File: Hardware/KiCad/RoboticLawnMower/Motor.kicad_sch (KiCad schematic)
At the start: 7 parts, among them J1 MOTOR, U1 INA233

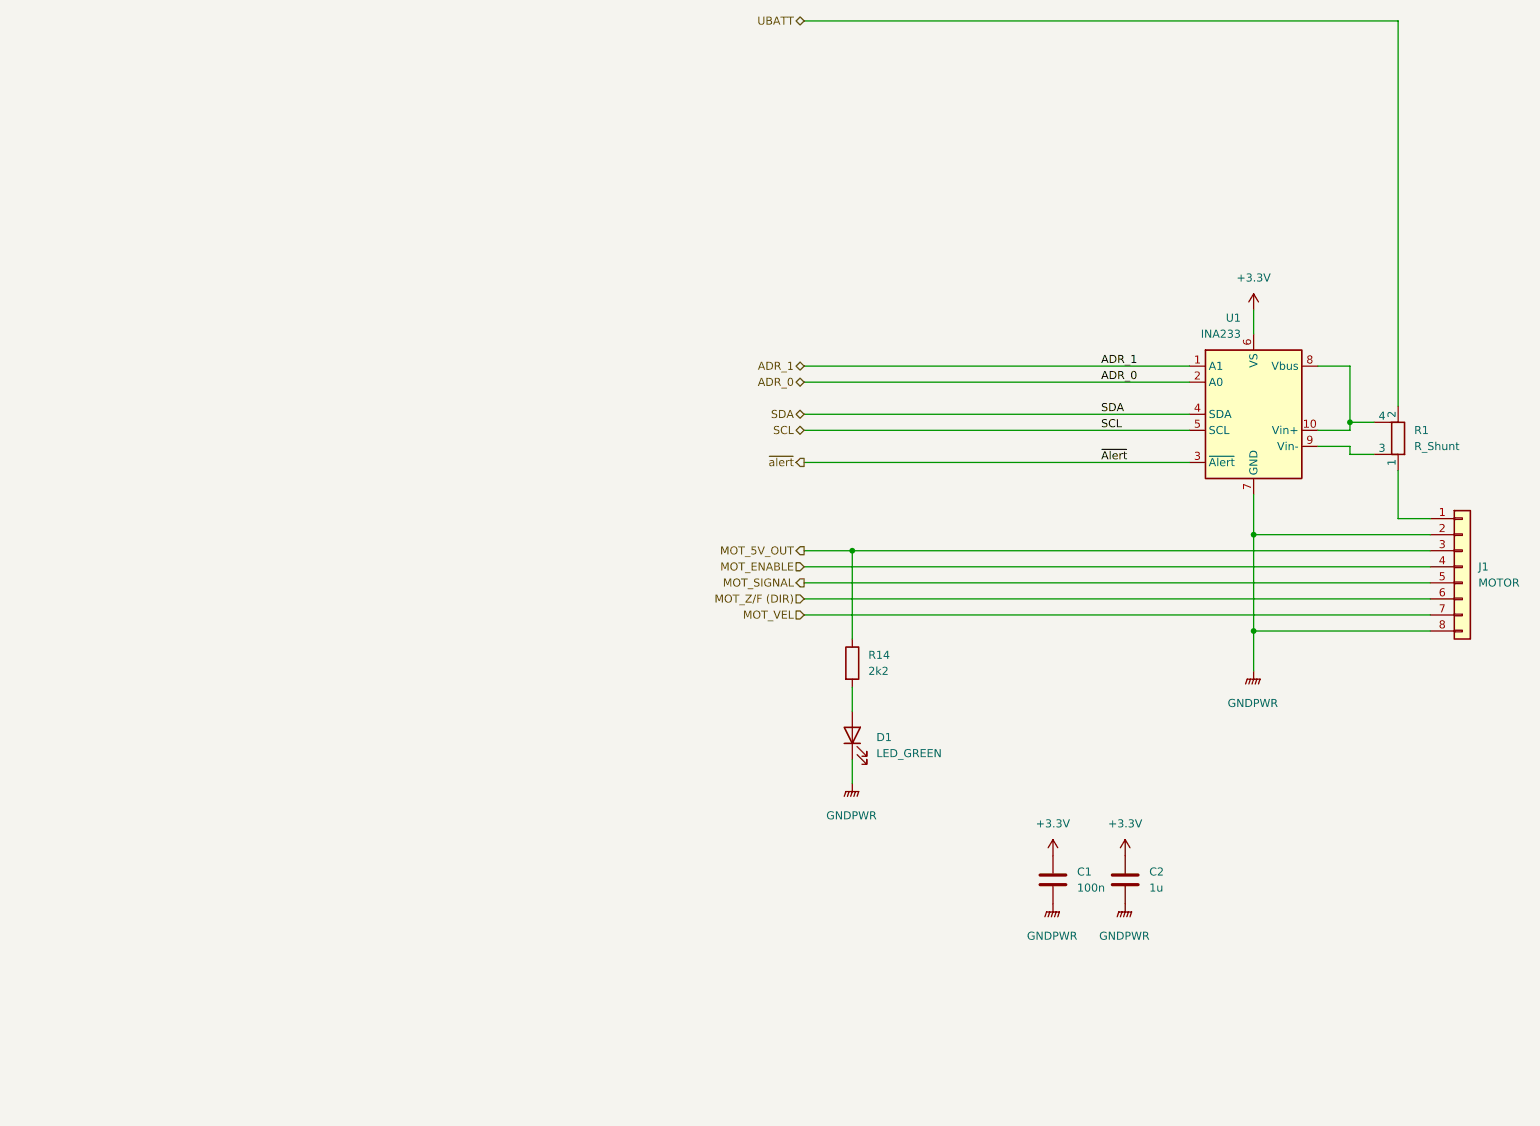
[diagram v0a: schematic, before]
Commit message: Redesign: - Controller - I2C pinning geändert - uvm
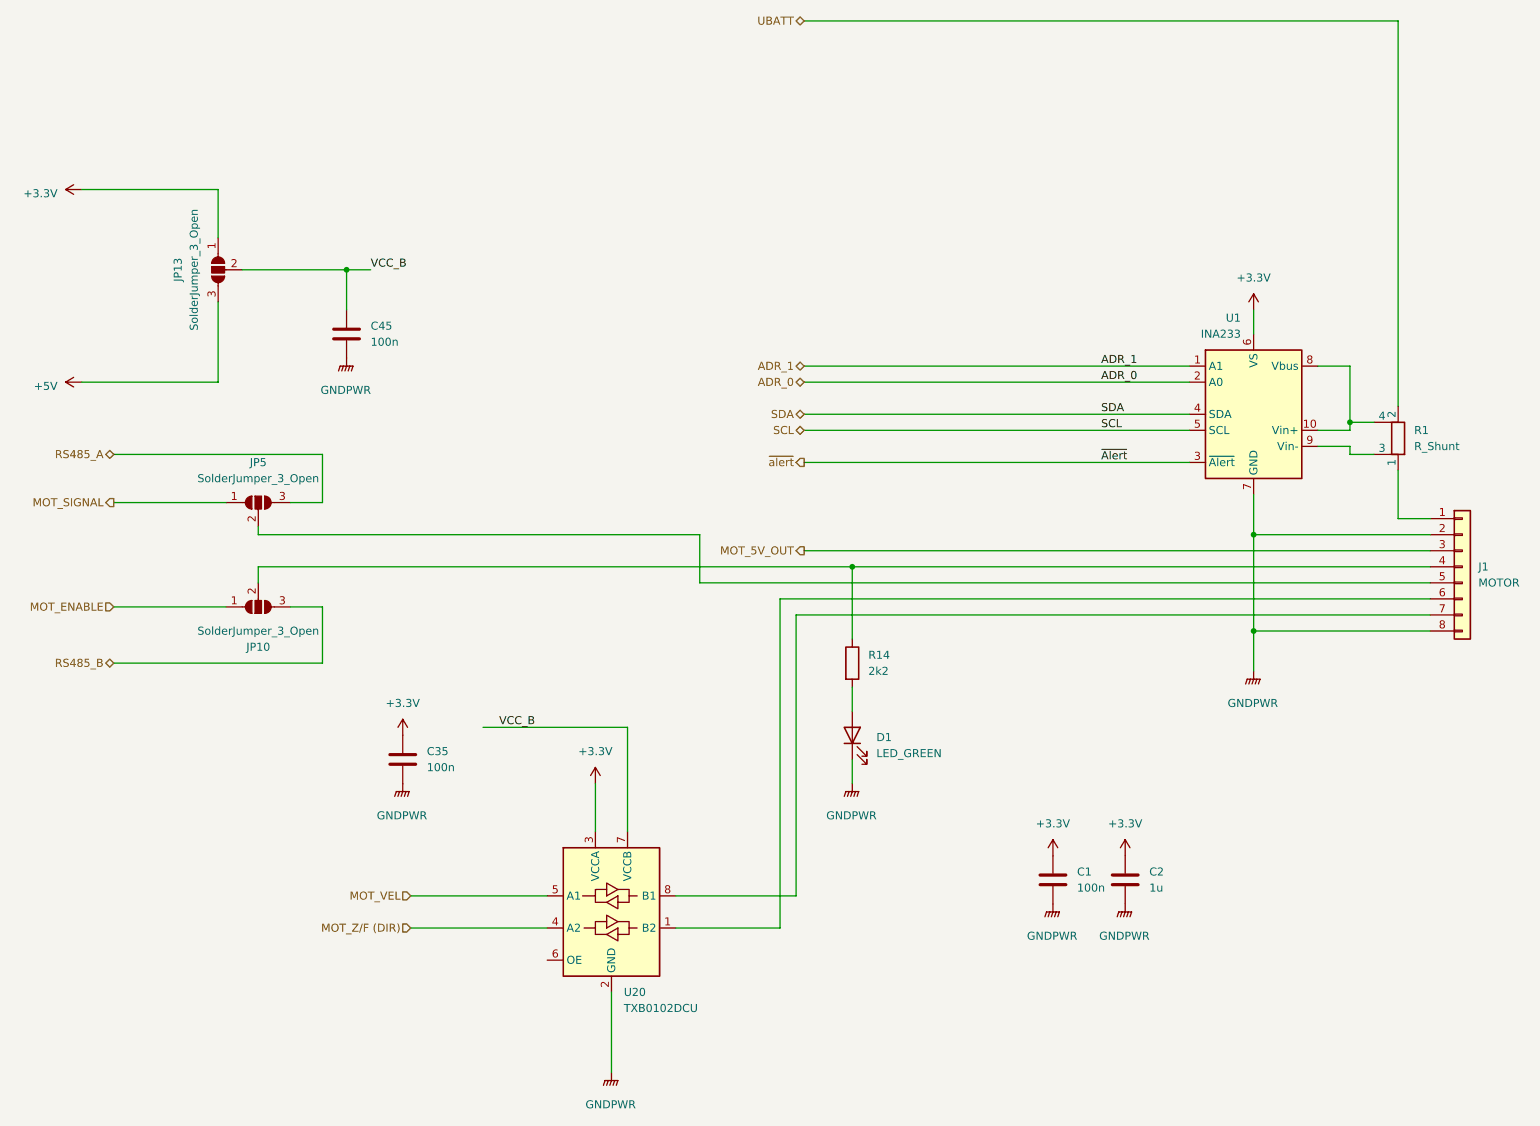
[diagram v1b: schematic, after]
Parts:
- added C35, C45: 100n, Capacitor_SMD:C_0603_1608Metric, symbol Device:C
- added JP10, JP13, JP5: SolderJumper_3_Open, Jumper:SolderJumper-3_P1.3mm_Open_RoundedPad1.0x1.5mm, symbol Jumper:SolderJumper_3_Open
- added U20: TXB0102DCU, Package_SO:VSSOP-8_2.4x2.1mm_P0.5mm, symbol Logic_LevelTranslator:TXB0102DCU
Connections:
- net +3.3V: now also C35.1, JP13.1 (A), U20.3 (VCCA)
- net GNDPWR: now also C35.2, C45.2, U20.2 (GND)
- net MOT_5V_OUT: no longer R14.1
- net MOT_ENABLE: now also JP10.1 (A); no longer J1.4 (Pin_4)
- net MOT_SIGNAL: now also JP5.1 (A); no longer J1.5 (Pin_5)
- net MOT_VEL: now also U20.5 (A1); no longer J1.7 (Pin_7)
- net MOT_Z/F (DIR): now also U20.4 (A2); no longer J1.6 (Pin_6)
- new net: J1.5 (Pin_5), JP5.2 (C)
- new net: J1.4 (Pin_4), JP10.2 (C), R14.1
- new net: J1.6 (Pin_6), U20.1 (B2)
- new net: J1.7 (Pin_7), U20.8 (B1)
- new net +5V: JP13.3 (B)
- new net RS485_A: JP5.3 (B)
- new net RS485_B: JP10.3 (B)
- new net VCC_B: C45.1, JP13.2 (C), U20.7 (VCCB)

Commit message: Layout fertig, Gerber-Datei muss noch erzeugt werden.
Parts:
- renumbered C2 to C10, C35 to C39, C45 to C49, C1 to C9, D1 to D5, J1 to J5, JP10 to JP12, JP13 to JP17, JP5 to JP7, R14 to R18, R1 to R5, U1 to U13, U20 to U24
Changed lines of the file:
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@@
 		(dnp no)
 		(fields_autoplaced yes)
-		(property "Reference" "C45"
+		(property "Reference" "C49"
 			(at 134.62 110.4899 0)
 			(effects
@@
 		(dnp no)
 		(fields_autoplaced yes)
-		(property "Reference" "#PWR060"
+		(property "Reference" "#PWR064"
 			(at 210.82 187.96 0)
 			(effects
@@
 		(dnp no)
 		(fields_autoplaced yes)
-		(property "Reference" "JP5"
+		(property "Reference" "JP7"
 			(at 116.84 132.08 0)
 			(effects
@@
 		(dnp no)
 		(fields_autoplaced yes)
-		(property "Reference" "D1"
+		(property "Reference" "D5"
 			(at 214.63 175.5774 90)
 			(effects
@@
 		(dnp no)
 		(fields_autoplaced yes)
-		(property "Reference" "#PWR0188"
+		(property "Reference" "#PWR0192"
 			(at 130.81 120.65 0)
 			(effects
@@
 		(dnp no)
 		(fields_autoplaced yes)
-		(property "Reference" "#PWR0168"
+		(property "Reference" "#PWR0176"
 			(at 139.7 179.07 0)
 			(effects
@@
 		(dnp no)
 		(fields_autoplaced yes)
-		(property "Reference" "#PWR0163"
+		(property "Reference" "#PWR0167"
 			(at 92.71 119.38 0)
 			(effects
@@
 		(on_board yes)
 		(dnp no)
-		(property "Reference" "JP10"
+		(property "Reference" "JP12"
 			(at 116.84 161.29 0)
 			(effects
@@
 		(dnp no)
 		(fields_autoplaced yes)
-		(property "Reference" "#PWR0169"
+		(property "Reference" "#PWR0177"
 			(at 139.7 187.96 0)
 			(effects
@@
 		(dnp no)
 		(fields_autoplaced yes)
-		(property "Reference" "C35"
+		(property "Reference" "C39"
 			(at 143.51 177.7999 0)
 			(effects
@@
 		(dnp no)
 		(fields_autoplaced yes)
-		(property "Reference" "#PWR0114"
+		(property "Reference" "#PWR0138"
 			(at 242.57 207.01 0)
 			(effects
@@
 		(dnp no)
 		(fields_autoplaced yes)
-		(property "Reference" "#PWR067"
+		(property "Reference" "#PWR087"
 			(at 170.18 186.69 0)
 			(effects
@@
 		(dnp no)
 		(fields_autoplaced yes)
-		(property "Reference" "#PWR098"
+		(property "Reference" "#PWR0162"
 			(at 92.71 88.9 0)
 			(effects
@@
 		(dnp no)
 		(fields_autoplaced yes)
-		(property "Reference" "#PWR0101"
+		(property "Reference" "#PWR0105"
 			(at 274.32 170.18 0)
 			(effects
@@
 		(dnp no)
 		(fields_autoplaced yes)
-		(property "Reference" "U20"
+		(property "Reference" "U24"
 			(at 174.6759 215.9 0)
 			(effects
@@
 		(dnp no)
 		(fields_autoplaced yes)
-		(property "Reference" "#PWR0115"
+		(property "Reference" "#PWR0139"
 			(at 242.57 198.12 0)
 			(effects
@@
 		(dnp no)
 		(fields_autoplaced yes)
-		(property "Reference" "R1"
+		(property "Reference" "R5"
 			(at 299.72 126.9999 0)
 			(effects
@@
 		(dnp no)
 		(fields_autoplaced yes)
-		(property "Reference" "C2"
+		(property "Reference" "C10"
 			(at 257.81 196.8499 0)
 			(effects
@@
 		(dnp no)
 		(fields_autoplaced yes)
-		(property "Reference" "#PWR0116"
+		(property "Reference" "#PWR0140"
 			(at 254 198.12 0)
 			(effects
@@
 		(dnp no)
 		(fields_autoplaced yes)
-		(property "Reference" "#PWR088"
+		(property "Reference" "#PWR092"
 			(at 172.72 233.68 0)
 			(effects
@@
 		(dnp no)
 		(fields_autoplaced yes)
-		(property "Reference" "#PWR0106"
+		(property "Reference" "#PWR0110"
 			(at 274.32 111.76 0)
 			(effects
@@
 		(dnp no)
 		(fields_autoplaced yes)
-		(property "Reference" "#PWR0113"
+		(property "Reference" "#PWR0137"
 			(at 254 207.01 0)
 			(effects
@@
 		(dnp no)
 		(fields_autoplaced yes)
-		(property "Reference" "R14"
+		(property "Reference" "R18"
 			(at 213.36 162.5599 0)
 			(effects
@@
 		(dnp no)
 		(fields_autoplaced yes)
-		(property "Reference" "U1"
+		(property "Reference" "U13"
 			(at 272.3006 109.22 0)
 			(effects
@@
 		(dnp no)
 		(fields_autoplaced yes)
-		(property "Reference" "J1"
+		(property "Reference" "J5"
 			(at 309.88 148.5899 0)
 			(effects
@@
 		(on_board yes)
 		(dnp no)
-		(property "Reference" "JP13"
+		(property "Reference" "JP17"
 			(at 104.14 101.6 0)
 			(effects
@@
 		(dnp no)
 		(fields_autoplaced yes)
-		(property "Reference" "C1"
+		(property "Reference" "C9"
 			(at 246.38 196.8499 0)
 			(effects

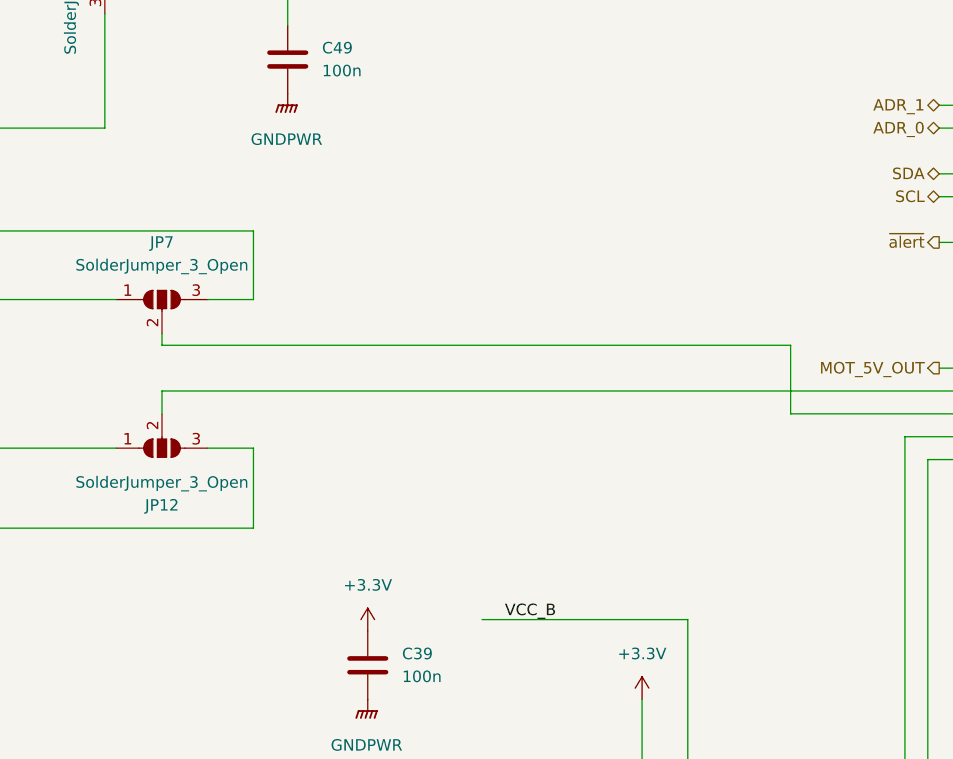
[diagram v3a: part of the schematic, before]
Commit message: Levelshift für MotorSignal zum µC
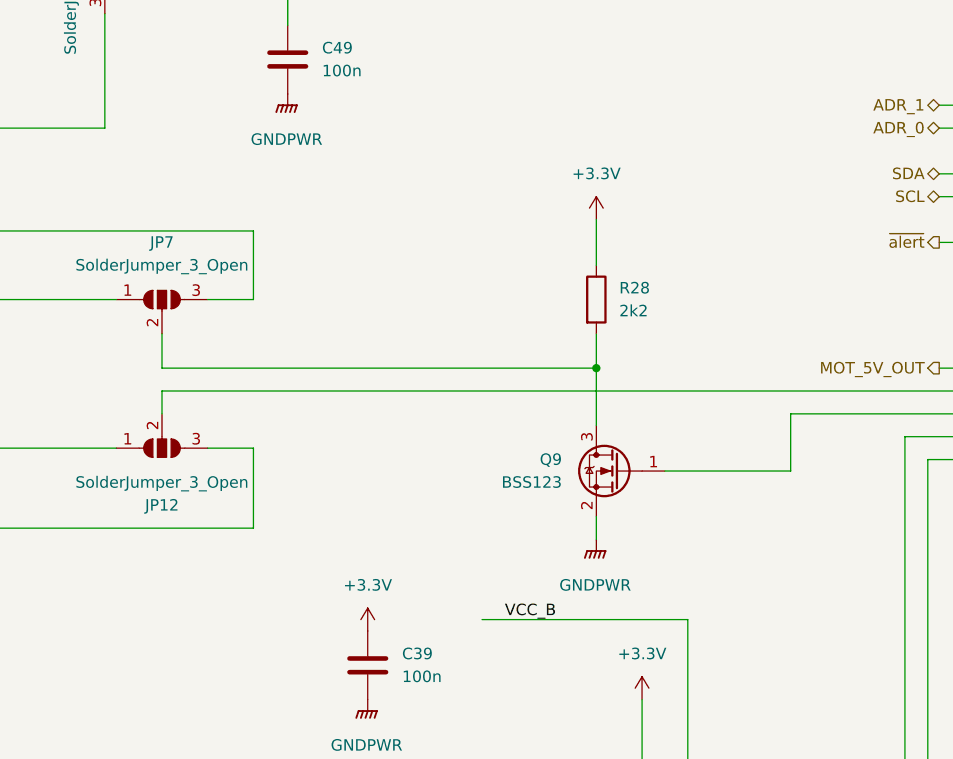
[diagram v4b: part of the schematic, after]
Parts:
- added Q9: BSS123, Package_TO_SOT_SMD:SOT-23, symbol Transistor_FET:BSS123
- added R28: 2k2, Resistor_SMD:R_0603_1608Metric, symbol Device:R
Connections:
- net +3.3V: now also R28.1
- net GNDPWR: now also Q9.2 (S)
- net at JP7.2 (C): now also Q9.3 (D), R28.2; no longer J5.5 (Pin_5)
- new net: J5.5 (Pin_5), Q9.1 (G)
